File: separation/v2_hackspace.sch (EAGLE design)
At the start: 16 parts

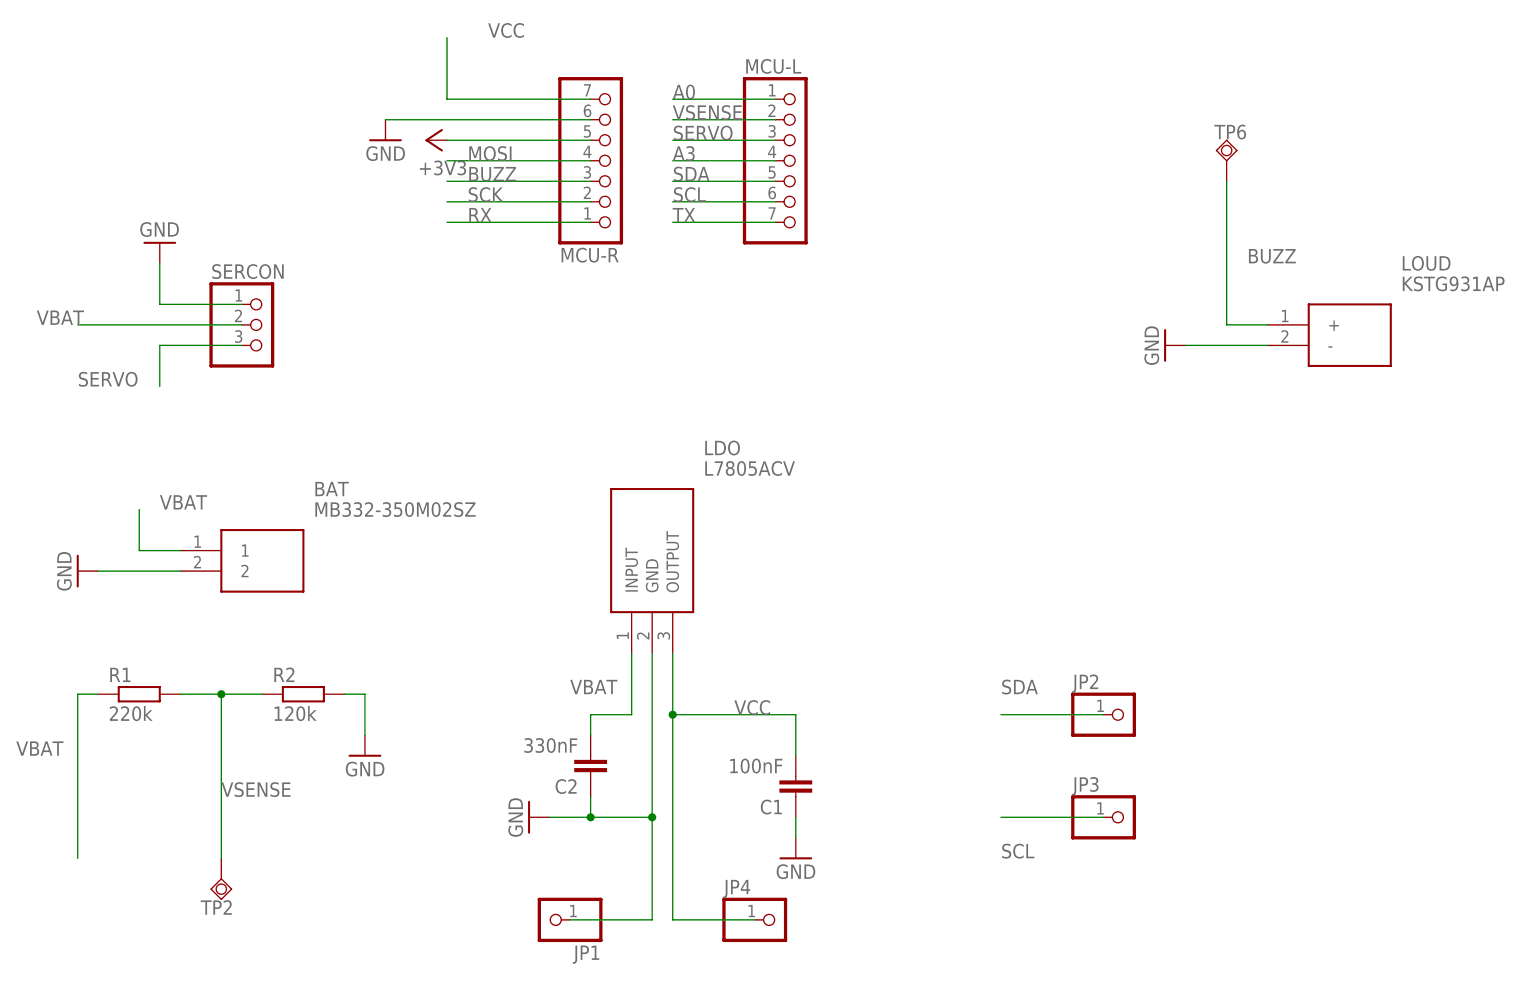
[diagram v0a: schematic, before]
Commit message: remove testpoints
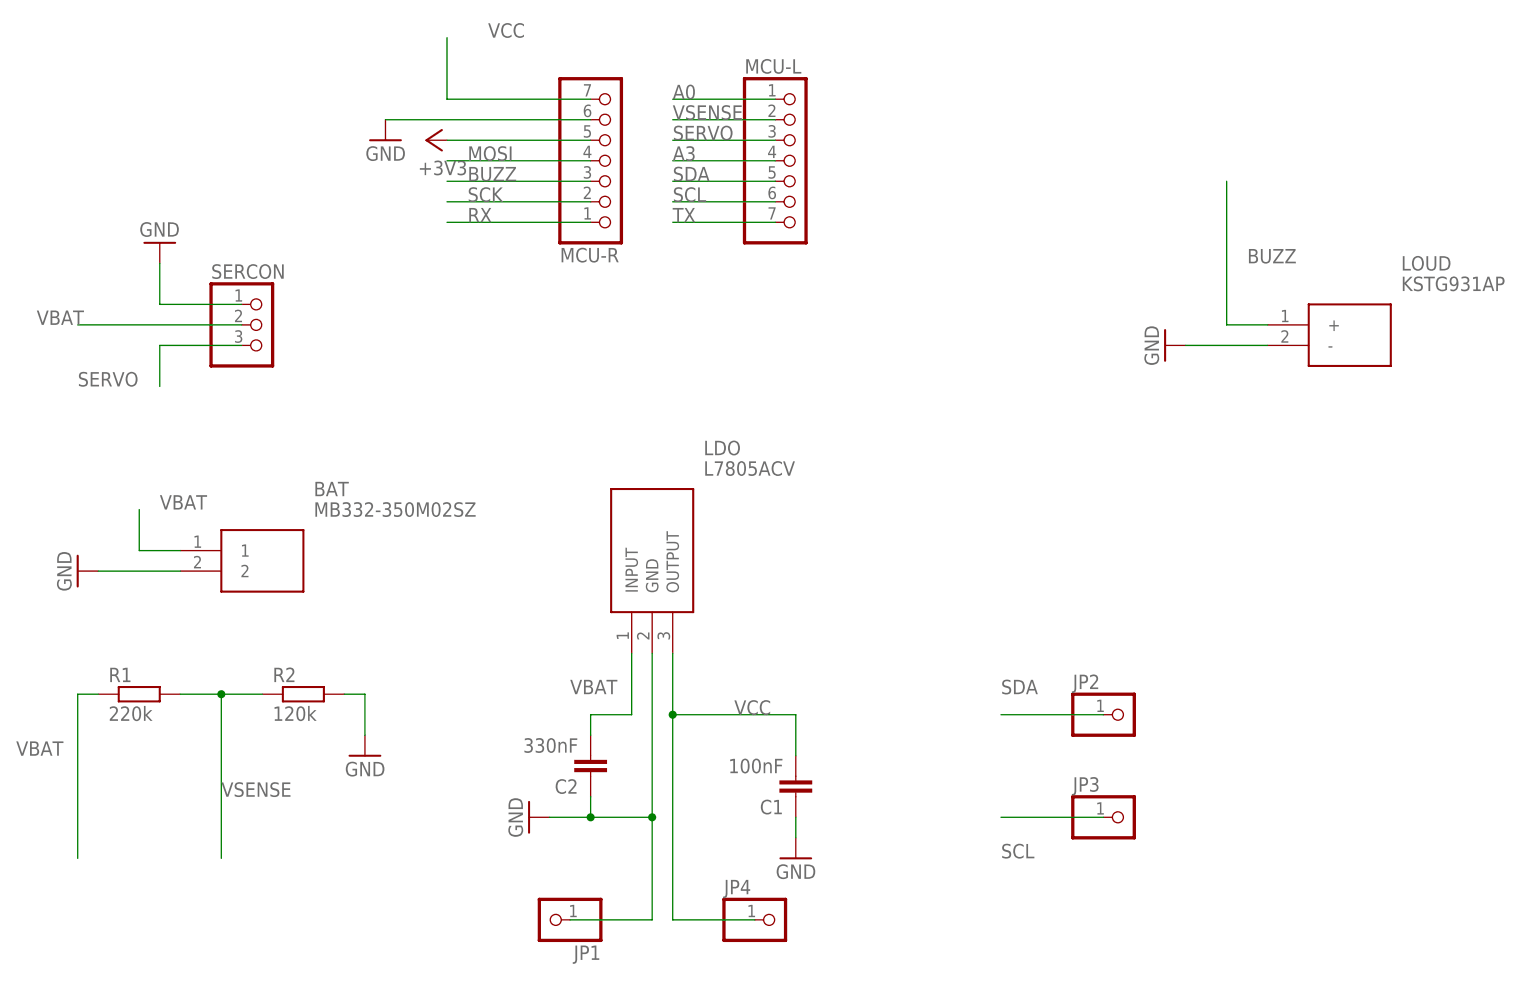
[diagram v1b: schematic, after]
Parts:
- removed TP2, TP6: TPSQB2,54, testpad:TPSQB2,54
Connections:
- net BUZZ: no longer TP6.TP
- net VSENSE: no longer TP2.TP
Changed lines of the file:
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@@
 <part name="R2" library="rcl" library_urn="urn:adsk.eagle:library:334" deviceset="R-EU_" device="0204/2V" package3d_urn="urn:adsk.eagle:package:23495/1" value="120k"/>
 <part name="GND6" library="supply1" library_urn="urn:adsk.eagle:library:371" deviceset="GND" device=""/>
-<part name="TP2" library="testpad" library_urn="urn:adsk.eagle:library:385" deviceset="TPSQ" device="B2,54" package3d_urn="urn:adsk.eagle:package:27948/1"/>
-<part name="TP6" library="testpad" library_urn="urn:adsk.eagle:library:385" deviceset="TPSQ" device="B2,54" package3d_urn="urn:adsk.eagle:package:27948/1"/>
 <part name="JP2" library="pinhead" library_urn="urn:adsk.eagle:library:325" deviceset="PINHD-1X1" device="" package3d_urn="urn:adsk.eagle:package:22485/2"/>
 <part name="JP3" library="pinhead" library_urn="urn:adsk.eagle:library:325" deviceset="PINHD-1X1" device="" package3d_urn="urn:adsk.eagle:package:22485/2"/>
@@
 <attribute name="VALUE" x="10.16" y="-17.78" size="1.778" layer="96" rot="MR0"/>
 </instance>
-<instance part="TP2" gate="G$1" x="-10.16" y="-30.48" smashed="yes">
-<attribute name="NAME" x="-12.7" y="-34.925" size="1.778" layer="95"/>
-<attribute name="TP_SIGNAL_NAME" x="-7.62" y="-31.75" size="1.778" layer="97"/>
-</instance>
-<instance part="TP6" gate="G$1" x="114.3" y="58.42" smashed="yes" rot="R180">
-<attribute name="NAME" x="116.84" y="62.865" size="1.778" layer="95" rot="R180"/>
-<attribute name="TP_SIGNAL_NAME" x="111.76" y="59.69" size="1.778" layer="97" rot="R180"/>
-</instance>
 <instance part="JP2" gate="G$1" x="101.6" y="-10.16" smashed="yes">
 <attribute name="NAME" x="95.25" y="-6.985" size="1.778" layer="95"/>
@@
 <wire x1="119.38" y1="38.1" x2="114.3" y2="38.1" width="0.1524" layer="91"/>
 <label x="116.84" y="45.72" size="1.778" layer="95"/>
-<pinref part="TP6" gate="G$1" pin="TP"/>
 <wire x1="114.3" y1="55.88" x2="114.3" y2="38.1" width="0.1524" layer="91"/>
 </segment>
@@
 <junction x="-10.16" y="-7.62"/>
 <label x="-10.16" y="-20.32" size="1.778" layer="95"/>
-<pinref part="TP2" gate="G$1" pin="TP"/>
 <wire x1="-10.16" y1="-27.94" x2="-10.16" y2="-7.62" width="0.1524" layer="91"/>
 </segment>

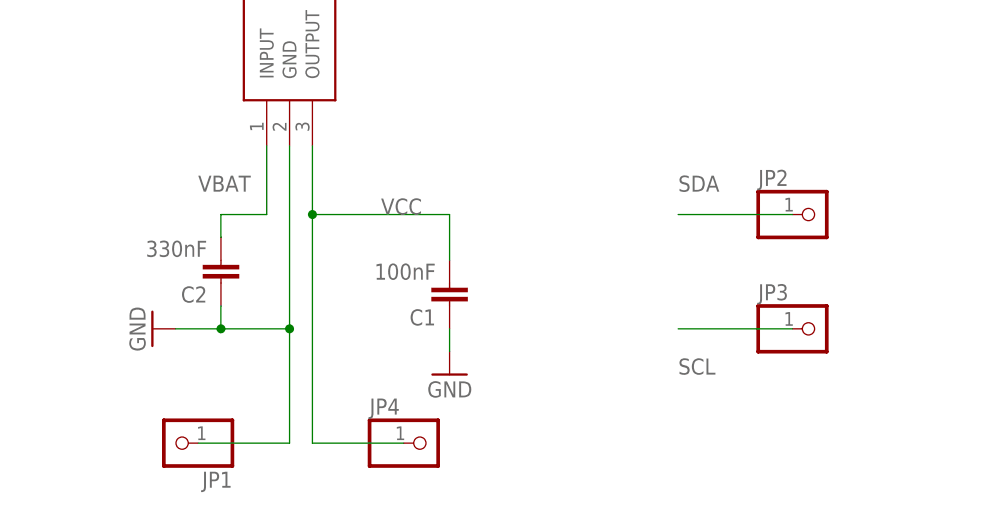
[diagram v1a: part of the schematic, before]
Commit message: remove spare breakouts
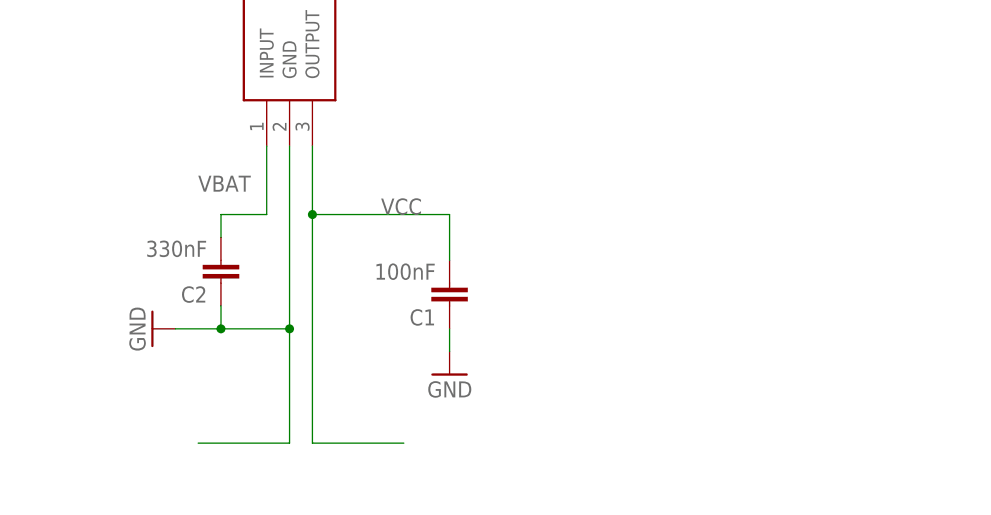
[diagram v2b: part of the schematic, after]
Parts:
- removed JP1, JP2, JP3, JP4: (no value), pinhead:PINHD-1X1
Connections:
- net GND: no longer JP1.1
- net SCL: no longer JP3.1
- net SDA: no longer JP2.1
- net VCC: no longer JP4.1
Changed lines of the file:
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@@
 <part name="R2" library="rcl" library_urn="urn:adsk.eagle:library:334" deviceset="R-EU_" device="0204/2V" package3d_urn="urn:adsk.eagle:package:23495/1" value="120k"/>
 <part name="GND6" library="supply1" library_urn="urn:adsk.eagle:library:371" deviceset="GND" device=""/>
-<part name="JP2" library="pinhead" library_urn="urn:adsk.eagle:library:325" deviceset="PINHD-1X1" device="" package3d_urn="urn:adsk.eagle:package:22485/2"/>
-<part name="JP3" library="pinhead" library_urn="urn:adsk.eagle:library:325" deviceset="PINHD-1X1" device="" package3d_urn="urn:adsk.eagle:package:22485/2"/>
-<part name="JP1" library="pinhead" library_urn="urn:adsk.eagle:library:325" deviceset="PINHD-1X1" device="" package3d_urn="urn:adsk.eagle:package:22485/2"/>
-<part name="JP4" library="pinhead" library_urn="urn:adsk.eagle:library:325" deviceset="PINHD-1X1" device="" package3d_urn="urn:adsk.eagle:package:22485/2"/>
 <part name="C1" library="rcl" library_urn="urn:adsk.eagle:library:334" deviceset="C-EU" device="025-024X044" package3d_urn="urn:adsk.eagle:package:23630/1" value="100nF"/>
 <part name="C2" library="rcl" library_urn="urn:adsk.eagle:library:334" deviceset="C-EU" device="025-024X044" package3d_urn="urn:adsk.eagle:package:23630/1" value="330nF"/>
@@
 <attribute name="VALUE" x="10.16" y="-17.78" size="1.778" layer="96" rot="MR0"/>
 </instance>
-<instance part="JP2" gate="G$1" x="101.6" y="-10.16" smashed="yes">
-<attribute name="NAME" x="95.25" y="-6.985" size="1.778" layer="95"/>
-<attribute name="VALUE" x="95.25" y="-15.24" size="1.778" layer="96"/>
-</instance>
-<instance part="JP3" gate="G$1" x="101.6" y="-22.86" smashed="yes">
-<attribute name="NAME" x="95.25" y="-19.685" size="1.778" layer="95"/>
-<attribute name="VALUE" x="95.25" y="-27.94" size="1.778" layer="96"/>
-</instance>
-<instance part="JP1" gate="G$1" x="30.48" y="-35.56" smashed="yes" rot="R180">
-<attribute name="NAME" x="36.83" y="-38.735" size="1.778" layer="95" rot="R180"/>
-<attribute name="VALUE" x="36.83" y="-30.48" size="1.778" layer="96" rot="R180"/>
-</instance>
-<instance part="JP4" gate="G$1" x="58.42" y="-35.56" smashed="yes">
-<attribute name="NAME" x="52.07" y="-32.385" size="1.778" layer="95"/>
-<attribute name="VALUE" x="52.07" y="-40.64" size="1.778" layer="96"/>
-</instance>
 <instance part="C1" gate="G$1" x="60.96" y="-20.32" smashed="yes" rot="R180">
 <attribute name="NAME" x="59.436" y="-20.701" size="1.778" layer="95" rot="R180"/>
@@
 <wire x1="30.48" y1="-22.86" x2="35.56" y2="-22.86" width="0.1524" layer="91"/>
 <junction x="43.18" y="-22.86"/>
-<pinref part="JP1" gate="G$1" pin="1"/>
 <wire x1="35.56" y1="-22.86" x2="43.18" y2="-22.86" width="0.1524" layer="91"/>
 <wire x1="43.18" y1="-35.56" x2="33.02" y2="-35.56" width="0.1524" layer="91"/>
@@
 <label x="45.72" y="53.34" size="1.778" layer="95"/>
 </segment>
-<segment>
-<pinref part="JP3" gate="G$1" pin="1"/>
-<wire x1="99.06" y1="-22.86" x2="86.36" y2="-22.86" width="0.1524" layer="91"/>
-<label x="86.36" y="-27.94" size="1.778" layer="95"/>
-</segment>
 </net>
 <net name="SDA" class="0">
@@
 <wire x1="45.72" y1="55.88" x2="58.42" y2="55.88" width="0.1524" layer="91"/>
 <label x="45.72" y="55.88" size="1.778" layer="95"/>
-</segment>
-<segment>
-<pinref part="JP2" gate="G$1" pin="1"/>
-<wire x1="99.06" y1="-10.16" x2="86.36" y2="-10.16" width="0.1524" layer="91"/>
-<label x="86.36" y="-7.62" size="1.778" layer="95"/>
 </segment>
 </net>
@@
 <junction x="45.72" y="-10.16"/>
 <wire x1="45.72" y1="-10.16" x2="45.72" y2="-35.56" width="0.1524" layer="91"/>
-<pinref part="JP4" gate="G$1" pin="1"/>
 <wire x1="45.72" y1="-35.56" x2="55.88" y2="-35.56" width="0.1524" layer="91"/>
 <wire x1="45.72" y1="-10.16" x2="60.96" y2="-10.16" width="0.1524" layer="91"/>
